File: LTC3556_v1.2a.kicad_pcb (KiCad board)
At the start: 4 copper layers, 45.4 x 38 mm, 43 parts, among them J1 USB_B_Micro, J2 Conn_01x01_Pin, J3 Conn_01x01_Pin, J4 Conn_01x01_Pin, J5 Conn_01x01_Pin, J6 Conn_01x01_Pin, Q1 SI2333DS-T1-E3, SW1 SW_SPDT, U1 LTC3556EUFD_PBF

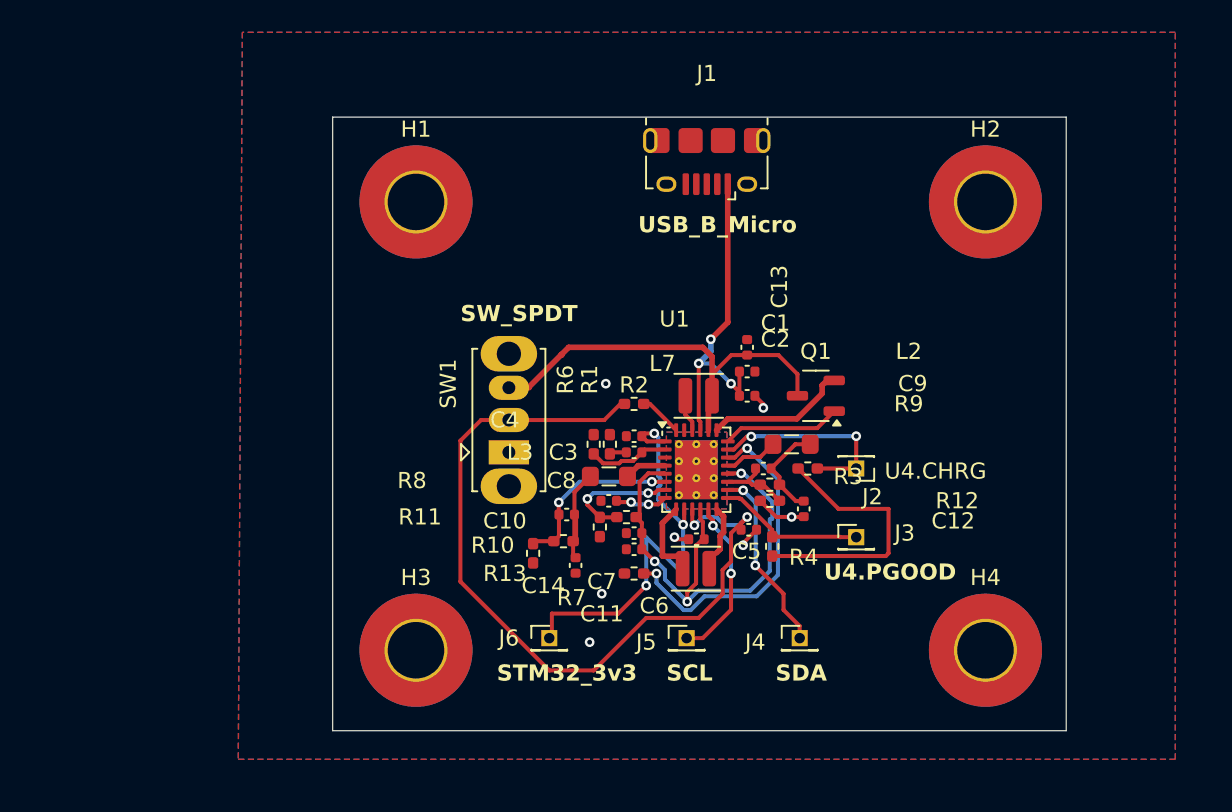
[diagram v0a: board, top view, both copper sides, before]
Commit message: Add files via upload
-Added TC7660EOA charge pump for AFE -2.5V AVSS
- Ppdated integration of both U1 and U2 IC's, V_Out I/O connections.
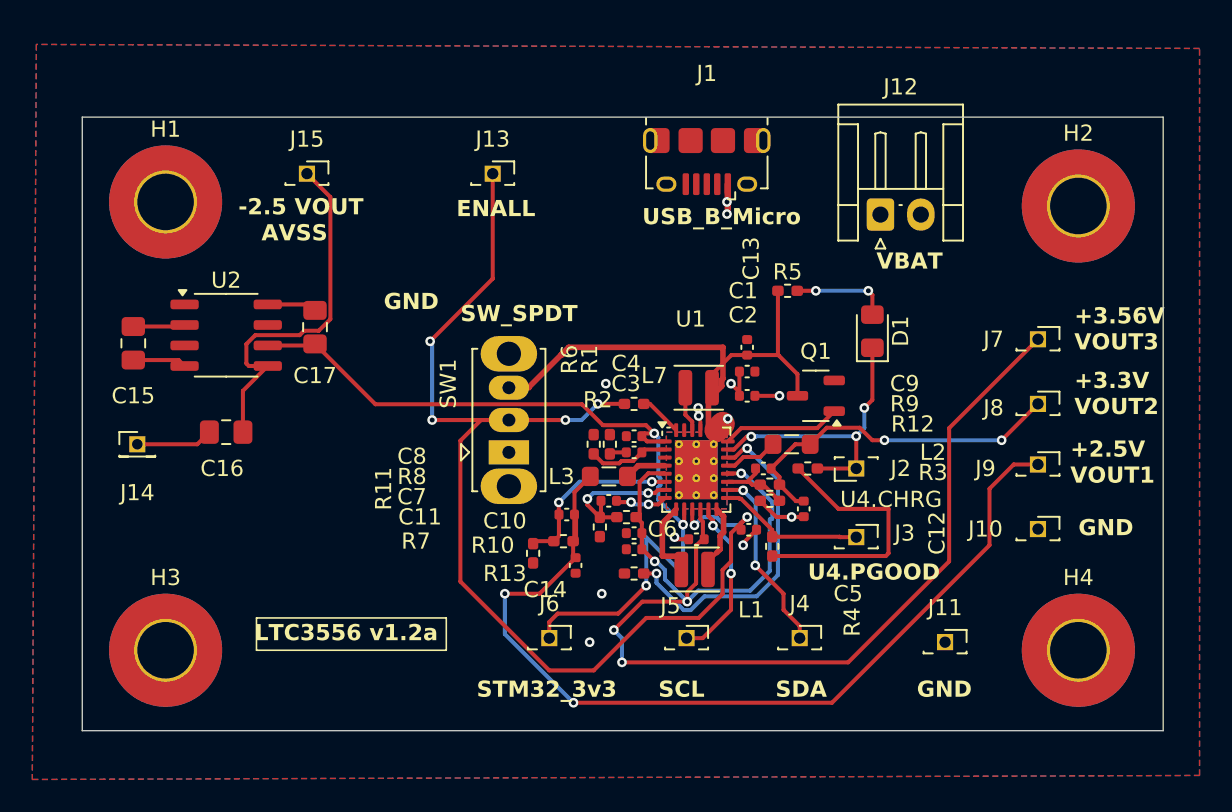
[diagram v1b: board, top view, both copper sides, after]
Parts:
- added C15: 10uF, Capacitor_SMD:C_0805_2012Metric_Pad1.18x1.45mm_HandSolder, F.Cu at (113.0, 86.8)
- added C16: 10uF, Capacitor_SMD:C_0805_2012Metric_Pad1.18x1.45mm_HandSolder, F.Cu at (118.8, 92.2)
- added C17: 10uF, Capacitor_SMD:C_0805_2012Metric_Pad1.18x1.45mm_HandSolder, F.Cu at (124.2, 85.8)
- added D1: LED, LED_SMD:LED_0805_2012Metric_Pad1.15x1.40mm_HandSolder, F.Cu at (158.8, 86.0)
- added J10: Conn_01x01_Pin, Connector_PinSocket_1.27mm:PinSocket_1x01_P1.27mm_Vertical, F.Cu at (169.0, 98.2)
- added J11: Conn_01x01_Pin, Connector_PinSocket_1.27mm:PinSocket_1x01_P1.27mm_Vertical, F.Cu at (163.2, 105.2)
- added J12: Conn_01x02_Pin, Connector_JST:JST_EH_S2B-EH_1x02_P2.50mm_Horizontal, F.Cu at (159.2, 78.8)
- added J13: Conn_01x01_Pin, Connector_PinSocket_1.27mm:PinSocket_1x01_P1.27mm_Vertical, F.Cu at (135.2, 76.2)
- added J14: Conn_01x01_Pin, Connector_PinHeader_1.27mm:PinHeader_1x01_P1.27mm_Vertical, F.Cu at (113.2, 93.0)
- added J15: Conn_01x01_Pin, Connector_PinSocket_1.27mm:PinSocket_1x01_P1.27mm_Vertical, F.Cu at (123.8, 76.2)
- added J7: Conn_01x01_Pin, Connector_PinSocket_1.27mm:PinSocket_1x01_P1.27mm_Vertical, F.Cu at (169.0, 86.5)
- added J8: Conn_01x01_Pin, Connector_PinSocket_1.27mm:PinSocket_1x01_P1.27mm_Vertical, F.Cu at (169.0, 90.5)
- added J9: Conn_01x01_Pin, Connector_PinSocket_1.27mm:PinSocket_1x01_P1.27mm_Vertical, F.Cu at (169.0, 94.2)
- added R5: 510, Resistor_SMD:R_0402_1005Metric_Pad0.72x0.64mm_HandSolder, F.Cu at (153.5, 83.5)
- added U2: ~, Package_SO:SO-8_3.9x4.9mm_P1.27mm, F.Cu at (118.8, 86.2)
- J2, J3, J4, J5, J6: footprint Connector_PinHeader_1.27mm:PinHeader_1x01_P1.27mm_Vertical -> Connector_PinSocket_1.27mm:PinSocket_1x01_P1.27mm_Vertical
- R10: value 365K -> 235K
- R9: value 365K -> 347K
- moved H1 15.5 mm to (115.0, 78.0)
- moved H3 15.5 mm to (115.0, 105.8)
- moved H2 5.76 mm to (171.5, 78.2)
- moved H4 5.75 mm to (171.5, 105.8)
- moved L7 0.50 mm to (148.0, 89.5)
- moved L1 0.09 mm to (147.8, 100.8)
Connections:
- net Net-(U1-VIN1) renamed VOUT3
- H1 pad 1: unconnected-(H1-Pad1) -> GND
- H2 pad 1: unconnected-(H2-Pad1) -> GND
- H3 pad 1: unconnected-(H3-Pad1) -> GND
- H4 pad 1: unconnected-(H4-Pad1) -> GND
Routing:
- net VOUT1: track 7.09 -> 57.6 mm, vias 0 -> 2
- net VOUT3: track 34.0 -> 80.1 mm
- net Net-(J6-Pin_1): track 27.3 -> 53.3 mm
- net GND: track 6.50 -> 30.4 mm, vias 7 -> 12
- net Net-(J15-Pin_1): track 0.00 -> 22.8 mm
- net VOUT0: track 51.3 -> 73.4 mm, vias 2 -> 6
- net VOUT2: track 6.18 -> 22.0 mm, vias 0 -> 2
- net Net-(J2-Pin_1): track 12.7 -> 0.00 mm, vias 2 -> 0
- net VBAT: track 8.86 -> 19.9 mm, vias 0 -> 1
- net Net-(D1-A): track 0.00 -> 5.98 mm, vias 0 -> 2
- net Net-(Q1-S): track 27.5 -> 32.8 mm
- net Net-(U2-CAP-): track 0.00 -> 3.33 mm
- net Net-(U2-CAP+): track 0.00 -> 3.22 mm
- net Net-(U2-V+): track 0.00 -> 3.08 mm
- net Net-(U1-FB3): track 7.54 -> 8.59 mm
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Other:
- board size 45.4 x 38 mm -> 66.9 x 38 mm
- board text added: "+2.5V VOUT1"
- board text added: "+3.3V VOUT2"
- board text added: "+3.56V VOUT3"
- board text added: "-2.5 VOUT AVSS"
- board text added: "ENALL"
- board text added: "GND"
- board text added: "LTC3556 v1.2a"
- board text added: "VBAT"

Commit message: Add files via upload
- PMIC, LTC3556 and charge Pump, TC7660EOA 98% completed
- Made corrections to 4-layer board, copper traces, via's grounds VOUT's vias corrections and ERC errors and warning corrections completed
- Added -2.5V AFE output for AVSS via (charge pump)
- will completed Gerber @ final step for JLCPCB
- We have the option for JLCPCB to assemble board for us
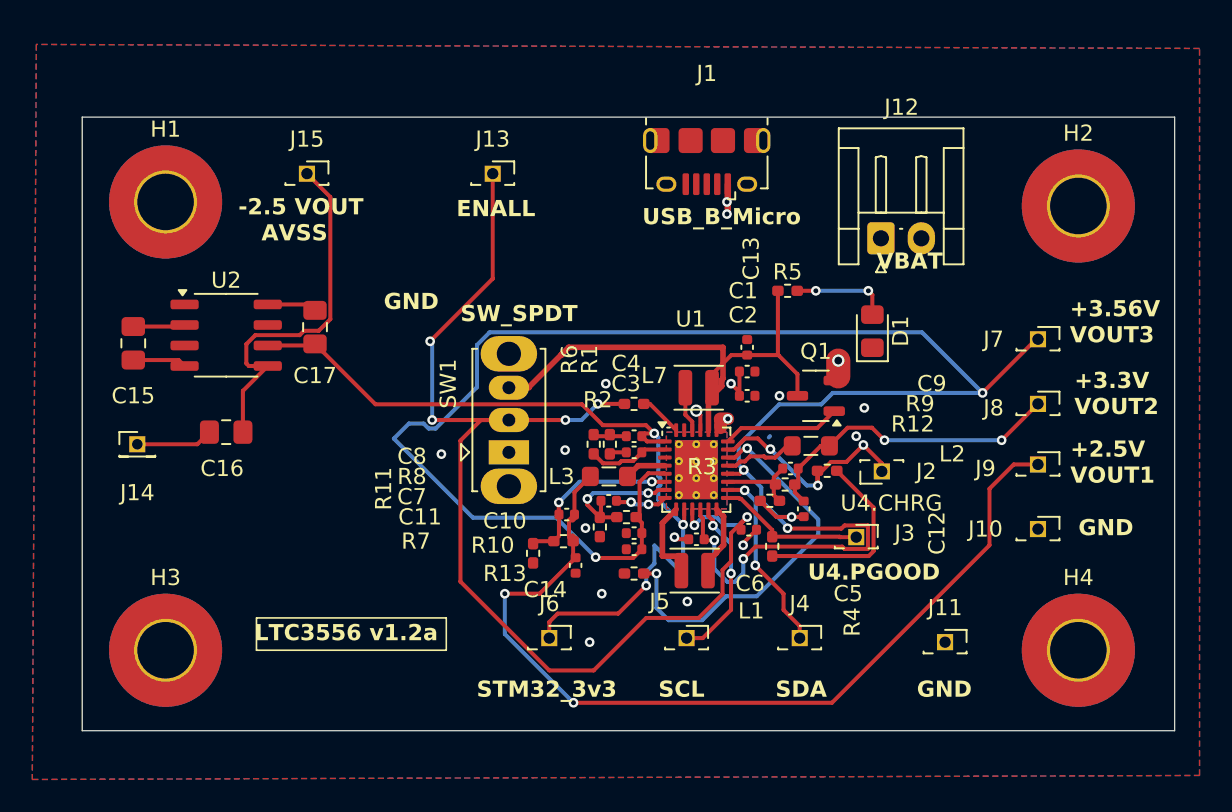
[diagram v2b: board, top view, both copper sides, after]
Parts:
- moved C9 1.68 mm to (153.7, 94.5)
- moved J2 1.60 mm to (159.3, 94.7)
- moved J12 1.47 mm to (159.3, 80.3)
- moved R3 1.21 mm to (155.9, 94.6), turned to 180 degrees
- moved L2 1.19 mm to (154.9, 93.1)
- moved R9 0.95 mm to (153.3, 95.5)
- moved L1 0.07 mm to (147.8, 100.8)
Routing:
- net VOUT3: track 80.1 -> 118.1 mm, vias 3 -> 6
- net GND: track 30.4 -> 12.5 mm, vias 12 -> 13
- net Net-(J2-Pin_1): track 0.00 -> 14.5 mm, vias 0 -> 3
- net VCC: track 16.7 -> 12.3 mm
- net Net-(U1-PROG): track 20.6 -> 24.0 mm
- net VOUT2: track 22.0 -> 19.5 mm
- net Net-(J6-Pin_1): track 53.3 -> 52.3 mm
- net Net-(U1-SW2): track 3.35 -> 4.34 mm
- net Net-(J1-VBUS): track 21.0 -> 21.7 mm, vias 5 -> 4
- net Net-(U1-FB2): track 4.60 -> 5.35 mm
- net VOUT1: track 57.6 -> 57.0 mm
- net VBAT: track 19.9 -> 19.8 mm, vias 1 -> 2
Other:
- board size 66.9 x 38 mm -> 67.6 x 38 mm
